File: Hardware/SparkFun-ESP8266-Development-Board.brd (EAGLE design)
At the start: 55.3 x 25.9 mm, 73 parts, among them J1 U.FL, Q1 2.5A/30V, U1 ESP8266, U2 MCP73831, U3 AT25SF041-SOIC8, U4 AP2112K-3.3V, U5 ATECC108-MAHDA, U6 TMP1021:1, U7 TSL2561FN, Y1 26MHz

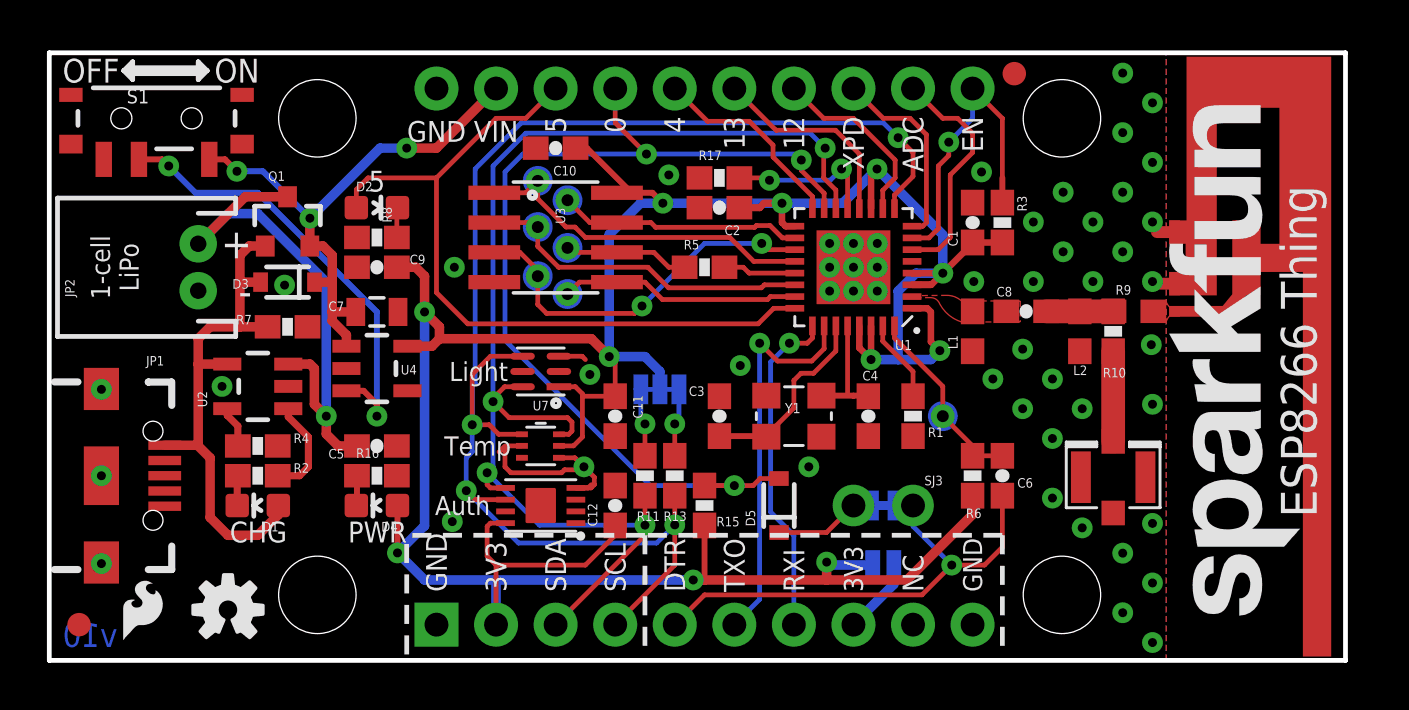
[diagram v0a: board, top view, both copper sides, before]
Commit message: Removing silk labels on sensors. Changing R4 to 2k (charge at 500mA).
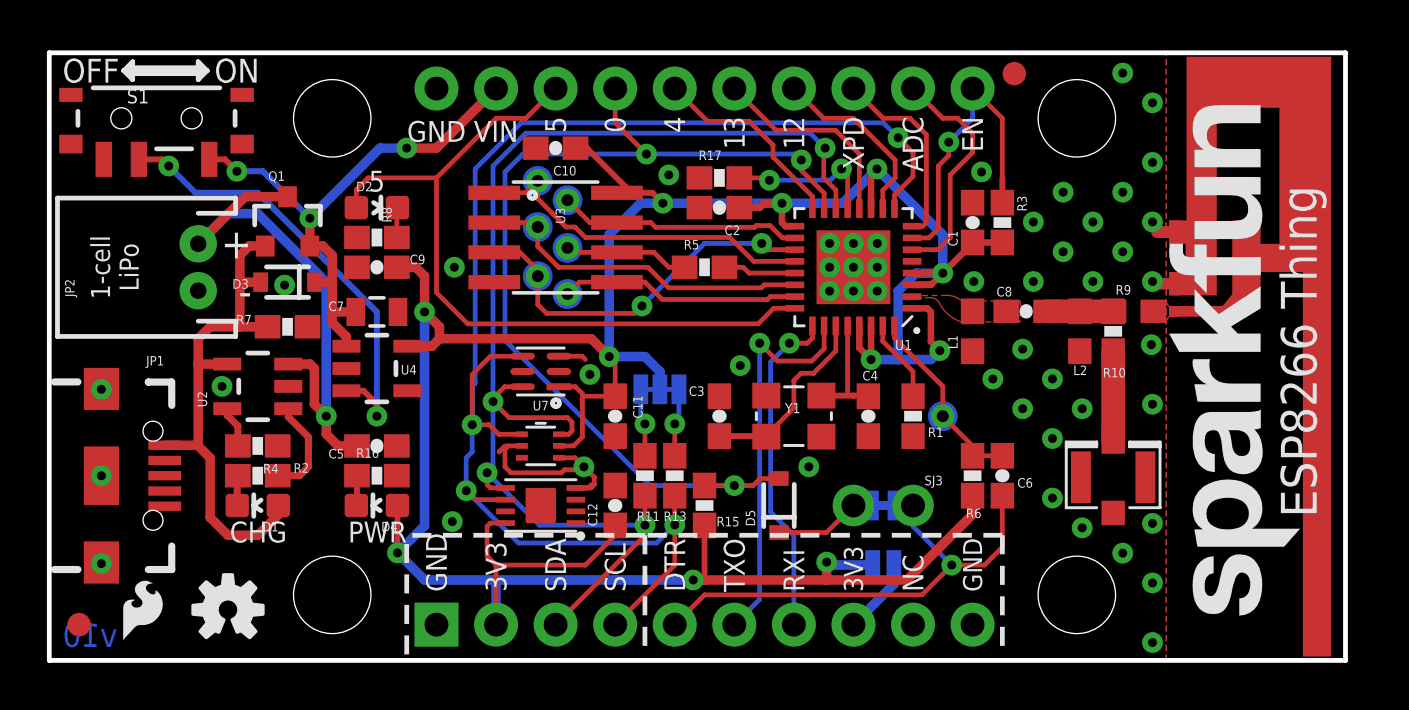
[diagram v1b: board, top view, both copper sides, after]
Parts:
- J1: value U.FL -> DNP
- R4: value 2.2k -> 2.0k
- moved STANDOFF3 0.63 mm to (12.1, 22.9)
- moved STANDOFF4 0.63 mm to (12.1, 2.54)
- moved STANDOFF1 0.63 mm to (43.8, 22.9)
- moved STANDOFF2 0.63 mm to (43.8, 2.54)
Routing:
- net GND: vias 52 -> 50
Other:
- board text removed: "Auth"
- board text removed: "Light"
- board text removed: "Temp"
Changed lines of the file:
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@@
 <layer number="223" name="223bmp" color="24" fill="1" visible="no" active="no"/>
 <layer number="224" name="224bmp" color="25" fill="1" visible="no" active="no"/>
+<layer number="225" name="225bmp" color="7" fill="1" visible="yes" active="yes"/>
+<layer number="226" name="226bmp" color="7" fill="1" visible="yes" active="yes"/>
+<layer number="227" name="227bmp" color="7" fill="1" visible="yes" active="yes"/>
+<layer number="228" name="228bmp" color="7" fill="1" visible="yes" active="yes"/>
+<layer number="229" name="229bmp" color="7" fill="1" visible="yes" active="yes"/>
+<layer number="230" name="230bmp" color="7" fill="1" visible="yes" active="yes"/>
+<layer number="231" name="231bmp" color="7" fill="1" visible="yes" active="yes"/>
 <layer number="248" name="Housing" color="7" fill="1" visible="no" active="yes"/>
 <layer number="249" name="Edge" color="7" fill="1" visible="no" active="yes"/>
@@
 <dimension x1="0" y1="-0.254" x2="55.2704" y2="-0.254" x3="27.6352" y3="-6.35" textsize="0.8636" textratio="15" layer="49" unit="inch"/>
 <dimension x1="10.16" y1="2.54" x2="10.16" y2="-0.254" x3="-2.54" y3="1.143" textsize="0.8636" textratio="15" layer="49" unit="inch"/>
-<dimension x1="11.43" y1="2.54" x2="0" y2="2.54" x3="5.715" y3="-2.286" textsize="0.8636" textratio="15" layer="49" unit="inch"/>
-<dimension x1="11.43" y1="22.86" x2="0" y2="22.86" x3="5.715" y3="28.956" textsize="0.8636" textratio="15" layer="49" unit="inch"/>
+<dimension x1="12.065" y1="2.54" x2="0" y2="2.54" x3="6.0325" y3="-2.286" textsize="0.8636" textratio="15" layer="49" unit="inch" precision="3"/>
+<dimension x1="12.065" y1="22.86" x2="0" y2="22.86" x3="6.0325" y3="28.956" textsize="0.8636" textratio="15" layer="49" unit="inch" precision="3"/>
 <dimension x1="10.16" y1="22.86" x2="10.16" y2="-0.254" x3="-4.572" y3="11.303" textsize="0.8636" textratio="15" layer="49" unit="inch"/>
 <dimension x1="16.51" y1="1.27" x2="16.51" y2="-0.254" x3="-0.508" y3="0.508" textsize="0.8636" textratio="15" layer="49" unit="inch"/>
@@
 <dimension x1="16.51" y1="1.27" x2="19.05" y2="1.27" x3="17.78" y3="-1.778" textsize="0.8636" textratio="15" layer="49" unit="inch"/>
 <dimension x1="16.51" y1="24.13" x2="0" y2="24.13" x3="8.255" y3="26.924" textsize="0.8636" textratio="15" layer="49" unit="inch"/>
-<dimension x1="43.18" y1="22.86" x2="0" y2="22.86" x3="21.59" y3="30.988" textsize="0.8636" textratio="15" layer="49" unit="inch"/>
-<dimension x1="43.18" y1="22.86" x2="44.831" y2="22.86" x3="44.0055" y3="27.686" textsize="0.8636" textratio="15" layer="49" unit="inch" precision="3"/>
+<dimension x1="43.815" y1="22.86" x2="0" y2="22.86" x3="21.9075" y3="30.988" textsize="0.8636" textratio="15" layer="49" unit="inch" precision="3"/>
+<dimension x1="43.815" y1="22.86" x2="45.466" y2="22.86" x3="44.6405" y3="27.686" textsize="0.8636" textratio="15" layer="49" unit="inch" precision="3"/>
 <text x="8.9154" y="5.6642" size="0.889" layer="21" font="vector" ratio="15" rot="R180" align="bottom-center">CHG</text>
 <text x="8.636" y="17.526" size="1.27" layer="21" font="vector" ratio="15" align="center-right">+</text>
@@
 <text x="31.75" y="2.794" size="0.889" layer="22" font="vector" ratio="15" rot="MR90" align="center-left">RXI</text>
 <text x="52.5145" y="5.842" size="1.524" layer="21" font="vector" ratio="15" rot="R90" align="top-left">ESP8266 Thing</text>
-<text x="19.685" y="8.89" size="0.8128" layer="21" font="vector" ratio="15" align="center-right">Temp</text>
-<text x="19.558" y="12.065" size="0.8128" layer="21" font="vector" ratio="15" align="center-right">Light</text>
 <wire x1="22.225" y1="7.1374" x2="22.479" y2="7.1374" width="0.0254" layer="41"/>
 <wire x1="21.59" y1="12.446" x2="21.844" y2="12.446" width="0.2032" layer="41"/>
 <wire x1="21.59" y1="8.3058" x2="21.844" y2="8.3058" width="0.0254" layer="41"/>
-<text x="18.796" y="6.35" size="0.8128" layer="21" font="vector" ratio="15" align="center-right">Auth</text>
 <text x="11.43" y="8.89" size="0.8128" layer="22" font="vector" ratio="15" rot="MR0" align="bottom-center">data.sparkfun.com</text>
 <wire x1="3.175" y1="24.892" x2="6.731" y2="24.892" width="0.2032" layer="21"/>
@@
 <wire x1="6.223" y1="24.765" x2="3.683" y2="24.765" width="0.2032" layer="21"/>
 <text x="3.81" y="16.51" size="0.8128" layer="21" font="vector" ratio="15" rot="R90" align="bottom-center">1-cell
+LiPo</text>
+<text x="3.81" y="16.51" size="0.8128" layer="22" font="vector" ratio="15" rot="MR270" align="bottom-center">1-cell
 LiPo</text>
 </plain>
@@
 <attribute name="VALUE" x="41.402" y="15.2645" size="0.4064" layer="27" font="vector"/>
 </element>
-<element name="J1" library="SparkFun-Connectors" package="U.FL" value="U.FL" x="45.3644" y="7.5565" smashed="yes" rot="R90">
+<element name="J1" library="SparkFun-Connectors" package="U.FL" value="DNP" x="45.3644" y="7.5565" smashed="yes" rot="R90">
 <attribute name="PROD_ID" value="CONN-09193" x="45.3644" y="7.5565" size="1.778" layer="27" font="vector" ratio="15" rot="R90" display="off"/>
 </element>
@@
 <attribute name="VALUE" x="4.1275" y="11.811" size="0.4064" layer="27"/>
 </element>
-<element name="R4" library="SparkFun-Resistors" package="0603-RES" value="2.2k" x="8.89" y="8.89" smashed="yes" rot="R180">
-<attribute name="PROD_ID" value="RES-08272" x="8.89" y="8.89" size="1.778" layer="27" font="vector" ratio="15" rot="R180" display="off"/>
-<attribute name="NAME" x="10.414" y="9.017" size="0.4064" layer="25" font="vector"/>
-<attribute name="VALUE" x="10.414" y="8.509" size="0.4064" layer="27" font="vector"/>
-</element>
 <element name="C5" library="SparkFun-Capacitors" package="0603-CAP" value="4.7uF" x="13.97" y="8.89" smashed="yes">
 <attribute name="PROD_ID" value="CAP-08280" x="13.97" y="8.89" size="1.778" layer="27" font="vector" ratio="15" display="off"/>
@@
 <attribute name="VALUE" x="45.9105" y="11.7094" size="0.4064" layer="27" font="vector" rot="R180"/>
 </element>
-<element name="STANDOFF3" library="SparkFun-Electromechanical" package="STAND-OFF" value="STAND-OFF" x="11.43" y="22.86"/>
-<element name="STANDOFF1" library="SparkFun-Electromechanical" package="STAND-OFF" value="STAND-OFF" x="43.18" y="22.86"/>
-<element name="STANDOFF2" library="SparkFun-Electromechanical" package="STAND-OFF" value="STAND-OFF" x="43.18" y="2.54"/>
-<element name="STANDOFF4" library="SparkFun-Electromechanical" package="STAND-OFF" value="STAND-OFF" x="11.43" y="2.54"/>
+<element name="STANDOFF3" library="SparkFun-Electromechanical" package="STAND-OFF" value="STAND-OFF" x="12.065" y="22.86"/>
+<element name="STANDOFF1" library="SparkFun-Electromechanical" package="STAND-OFF" value="STAND-OFF" x="43.815" y="22.86"/>
+<element name="STANDOFF2" library="SparkFun-Electromechanical" package="STAND-OFF" value="STAND-OFF" x="43.815" y="2.54"/>
+<element name="STANDOFF4" library="SparkFun-Electromechanical" package="STAND-OFF" value="STAND-OFF" x="12.065" y="2.54"/>
 <element name="FID2" library="SparkFun-Aesthetics" package="FIDUCIAL-1X2" value="FIDUCIAL1X2" x="1.27" y="1.27"/>
 <element name="FID1" library="SparkFun-Aesthetics" package="FIDUCIAL-1X2" value="FIDUCIAL1X2" x="41.148" y="24.765"/>
@@
 </element>
 <element name="SJ1" library="SparkFun-Passives" package="PAD-JUMPER-2-NC_BY_TRACE_YES_SILK" value="" x="35.56" y="6.35" rot="MR180"/>
+<element name="R4" library="SparkFun-Resistors" package="0603-RES" value="2.0k" x="8.89" y="8.89" rot="R180">
+<attribute name="PROD_ID" value="RES-08296" x="8.89" y="8.89" size="1.778" layer="27" font="vector" ratio="15" rot="R180" display="off"/>
+</element>
 </elements>
 <signals>
@@
 <contactref element="JP1" pad="SHIELD2"/>
 <contactref element="U2" pad="2"/>
-<contactref element="R4" pad="1"/>
 <contactref element="C5" pad="2"/>
 <contactref element="R7" pad="1"/>
@@
 <via x="47.0408" y="23.5204" extent="1-16" drill="0.381"/>
 <via x="45.7708" y="24.7904" extent="1-16" drill="0.381"/>
-<via x="45.7708" y="22.2504" extent="1-16" drill="0.381"/>
 <via x="45.7708" y="19.7104" extent="1-16" drill="0.381"/>
 <via x="45.7708" y="17.1704" extent="1-16" drill="0.381"/>
 <via x="45.7708" y="4.318" extent="1-16" drill="0.381"/>
-<via x="45.7708" y="1.778" extent="1-16" drill="0.381"/>
 <via x="43.2308" y="19.7104" extent="1-16" drill="0.381"/>
 <via x="41.9608" y="18.4404" extent="1-16" drill="0.381"/>
@@
 <wire x1="19.431" y1="8.001" x2="19.685" y2="7.747" width="0.2032" layer="1"/>
 <contactref element="C12" pad="2"/>
+<contactref element="R4" pad="1"/>
 </signal>
 <signal name="N$1">
@@
 <wire x1="16.51" y1="21.59" x2="19.05" y2="24.13" width="0.4064" layer="1"/>
 <wire x1="12.065" y1="15.875" x2="12.065" y2="14.605" width="0.4064" layer="1"/>
-<wire x1="12.065" y1="14.605" x2="12.065" y2="14.224" width="0.4064" layer="1"/>
-<wire x1="12.065" y1="14.224" x2="12.6699" y2="13.6191" width="0.4064" layer="1"/>
-<wire x1="12.6699" y1="13.142" x2="12.6699" y2="13.6191" width="0.4064" layer="1"/>
+<wire x1="12.065" y1="14.605" x2="12.065" y2="14.1478" width="0.4064" layer="1"/>
+<wire x1="12.065" y1="14.1478" x2="12.6699" y2="13.5429" width="0.4064" layer="1"/>
 <wire x1="13.07" y1="14.605" x2="12.065" y2="14.605" width="0.4064" layer="1"/>
 <wire x1="6.822" y1="21.11" x2="7.493" y2="21.11" width="0.254" layer="1"/>
@@
 <wire x1="11.1125" y1="18.6005" x2="11.1075" y2="18.6005" width="0.254" layer="16"/>
 <wire x1="11.1075" y1="18.6005" x2="9.106" y2="20.602" width="0.254" layer="16"/>
+<wire x1="12.6699" y1="13.142" x2="12.6699" y2="13.5429" width="0.4064" layer="1"/>
 </signal>
 <signal name="VUSB">
@@
 <signal name="N$14">
 <contactref element="U2" pad="5"/>
-<contactref element="R4" pad="2"/>
 <wire x1="8.04" y1="8.89" x2="8.04" y2="9.74" width="0.3048" layer="1"/>
 <wire x1="8.04" y1="9.74" x2="7.5899" y2="10.1901" width="0.3048" layer="1"/>
 <wire x1="7.5899" y1="10.48" x2="7.5899" y2="10.1901" width="0.3048" layer="1"/>
+<contactref element="R4" pad="2"/>
 </signal>
 <signal name="VBAT">

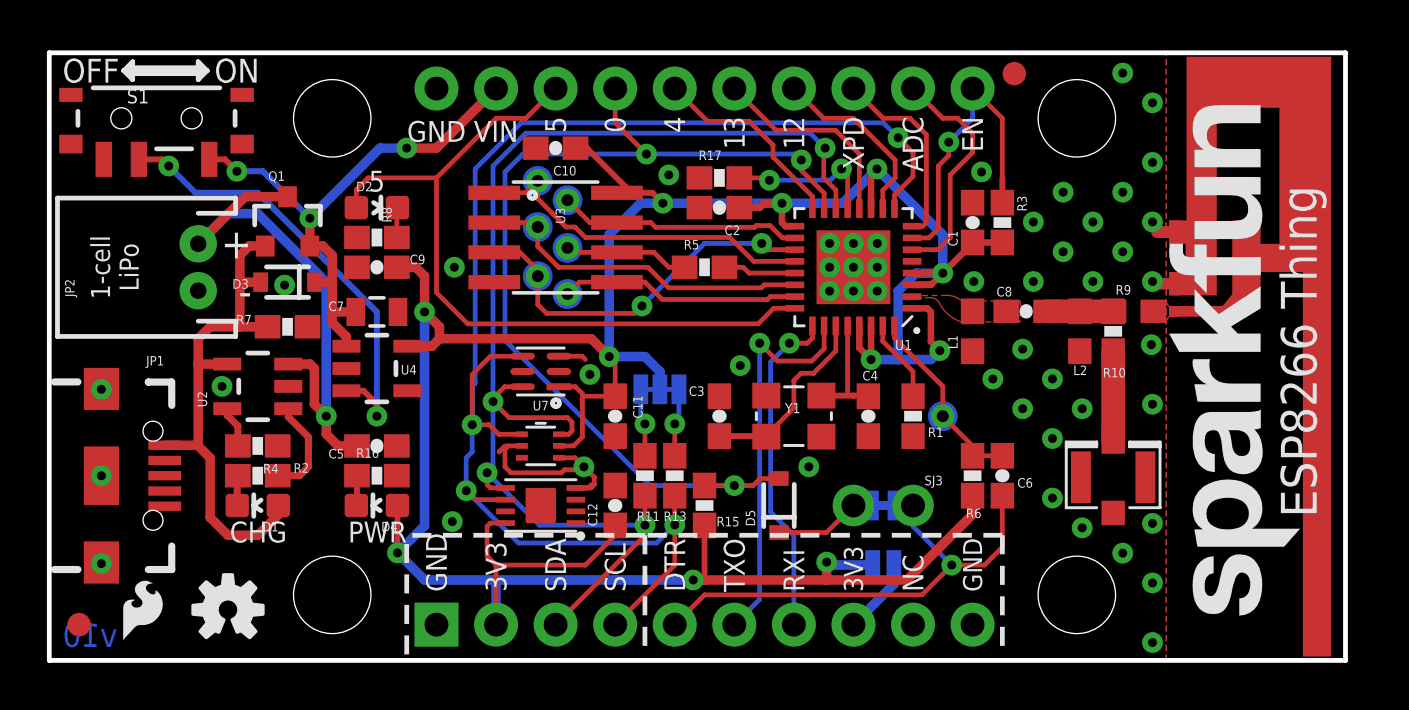
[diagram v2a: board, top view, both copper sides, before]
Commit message: Extending border dimension out to grid.
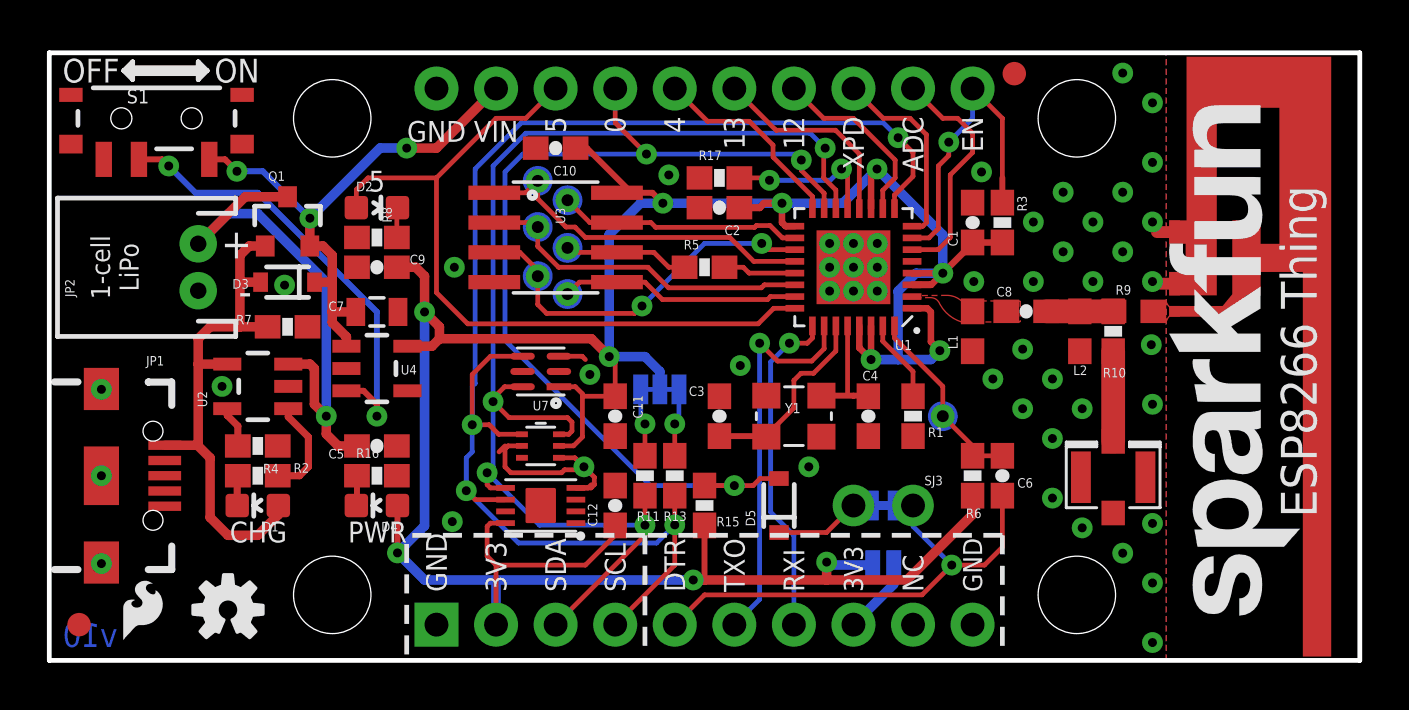
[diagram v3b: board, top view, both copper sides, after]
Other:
- board size 55.3 x 25.9 mm -> 55.9 x 25.9 mm
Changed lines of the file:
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@@
 <plain>
 <wire x1="0" y1="-0.254" x2="0" y2="25.654" width="0.2032" layer="20"/>
-<wire x1="0" y1="25.654" x2="55.2704" y2="25.654" width="0.2032" layer="20"/>
-<wire x1="55.2704" y1="25.654" x2="55.2704" y2="-0.254" width="0.2032" layer="20"/>
-<wire x1="55.2704" y1="-0.254" x2="0" y2="-0.254" width="0.2032" layer="20"/>
+<wire x1="0" y1="25.654" x2="55.88" y2="25.654" width="0.2032" layer="20"/>
+<wire x1="55.88" y1="25.654" x2="55.88" y2="-0.254" width="0.2032" layer="20"/>
+<wire x1="55.88" y1="-0.254" x2="0" y2="-0.254" width="0.2032" layer="20"/>
 <text x="24.13" y="2.667" size="0.889" layer="21" font="vector" ratio="15" rot="R90" align="center-left">SCL</text>
 <text x="21.59" y="2.667" size="0.889" layer="21" font="vector" ratio="15" rot="R90" align="center-left">SDA</text>
